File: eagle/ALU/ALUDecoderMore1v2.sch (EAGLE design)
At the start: 0 parts

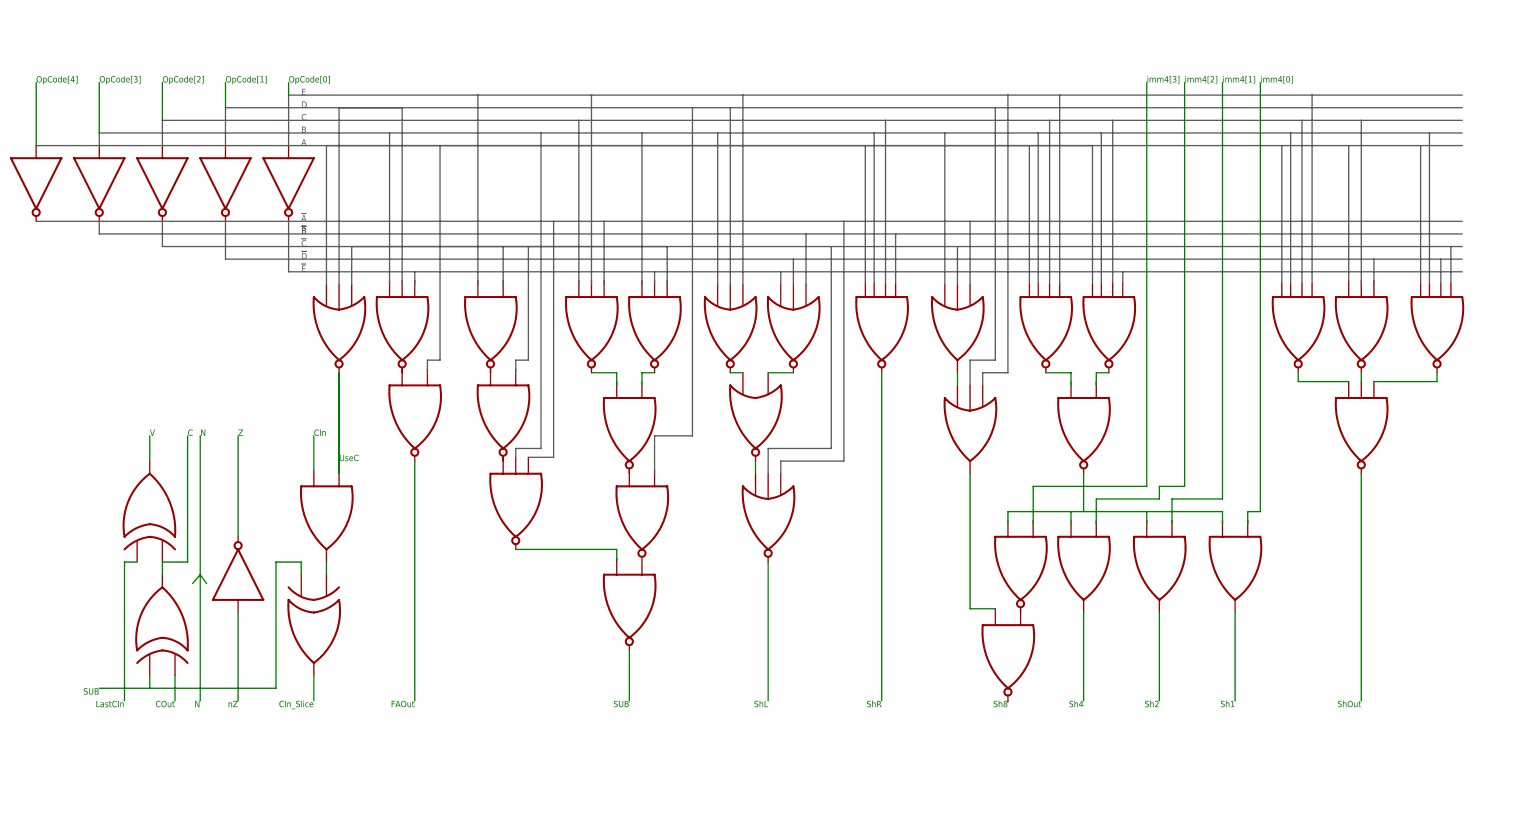
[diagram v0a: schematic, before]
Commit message: Eagle schematics now use library
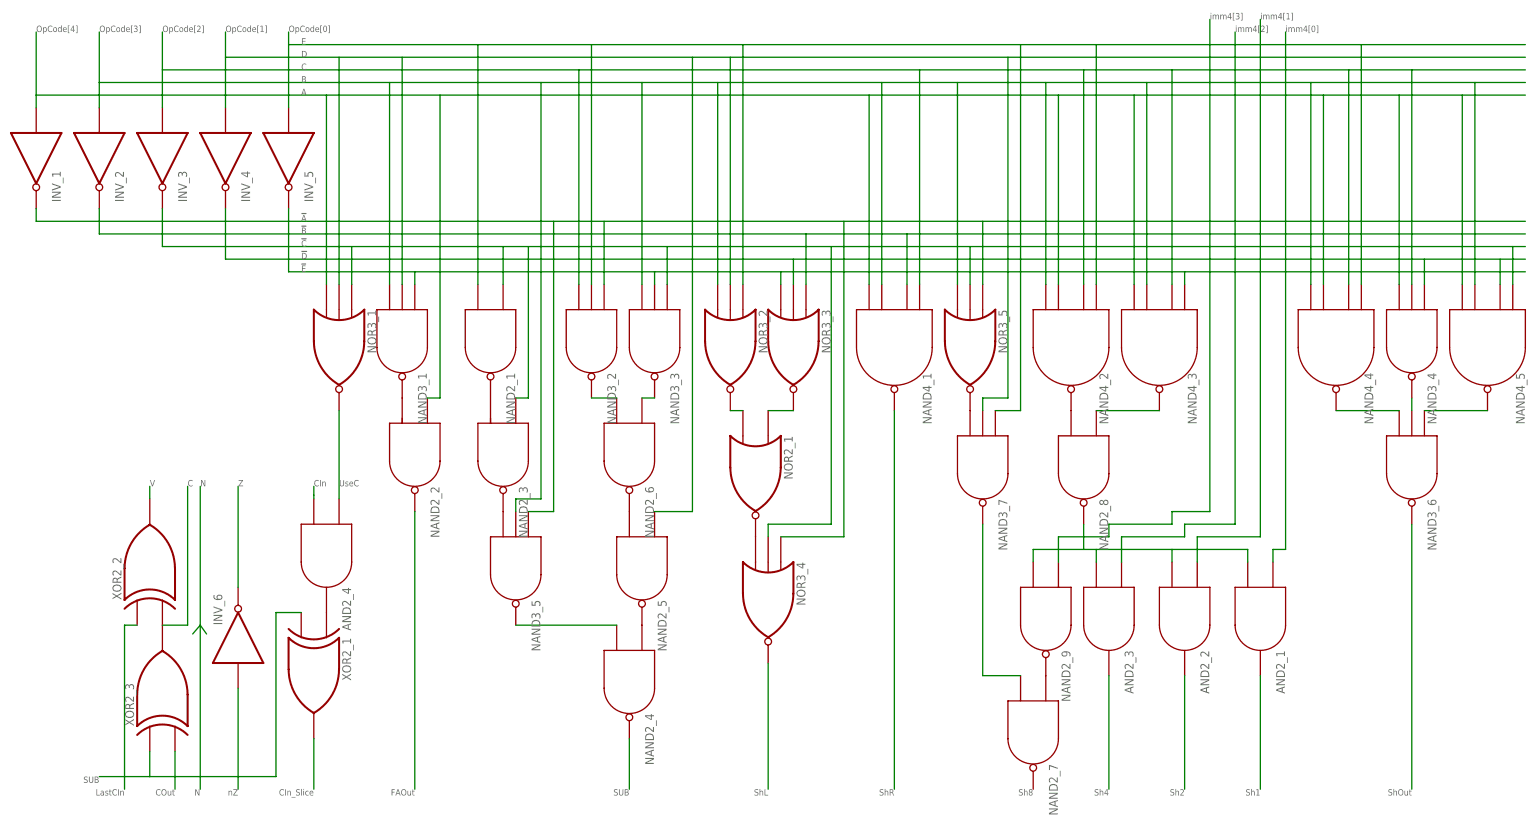
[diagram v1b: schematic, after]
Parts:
- added AND2_1, AND2_2, AND2_3, AND2_4: AND2, c035u:AND2
- added INV_1, INV_2, INV_3, INV_4, INV_5, INV_6: INV, c035u:INV
- added NAND2_1, NAND2_2, NAND2_3, NAND2_4, NAND2_5, NAND2_6, NAND2_7, NAND2_8, NAND2_9: NAND2, c035u:NAND2
- added NAND3_1, NAND3_2, NAND3_3, NAND3_4, NAND3_5, NAND3_6, NAND3_7: NAND3, c035u:NAND3
- added NAND4_1, NAND4_2, NAND4_3, NAND4_4, NAND4_5: NAND4, c035u:NAND4
- added NOR2_1: NOR2, c035u:NOR2
- added NOR3_1, NOR3_2, NOR3_3, NOR3_4, NOR3_5: NOR3, c035u:NOR3
- added XOR2_1, XOR2_2, XOR2_3: XOR2, c035u:XOR2
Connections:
- new net N$1: NAND2_1.O, NAND2_3.I1
- new net N$10: NOR2_1.I1, NOR3_2.O
- new net N$100: NAND4_4.A1
- new net N$101: NAND4_4.A
- new net N$102: NAND3_4.I1
- new net N$103: NAND3_4.I2
- new net N$104: NAND3_4.A
- new net N$105: NAND4_5.I2
- new net N$106: NAND4_5.I1
- new net N$107: NAND4_5.A1
- new net N$109: INV_2.O
- new net N$11: NOR2_1.O, NOR3_4.I1
- new net N$12: NAND2_8.I1, NAND4_2.O
- new net N$13: NAND2_8.A, NAND4_3.O
- new net N$14: NAND2_4.A, NAND2_5.O
- new net N$15: NAND2_4.O
- new net N$16: AND2_1.I1, AND2_2.I1, AND2_3.I1, NAND2_8.O, NAND2_9.I1
- new net N$17: NAND3_6.I1, NAND4_4.O
- new net N$18: NAND3_4.O, NAND3_6.I2
- new net N$19: NOR3_4.O
- new net N$2: INV_1.I
- new net N$20: NAND3_6.A, NAND4_5.O
- new net N$22: NAND3_7.I1, NOR3_5.O
- new net N$24: NAND2_9.A
- new net N$25: XOR2_2.O
- new net N$27: NAND2_7.I1, NAND3_7.O
- new net N$28: AND2_3.A
- new net N$29: AND2_2.A
- new net N$3: NAND2_2.I1, NAND3_1.O
- new net N$30: AND2_1.A
- new net N$31: AND2_3.O
- new net N$32: AND2_2.O
- new net N$33: AND2_1.O
- new net N$35: INV_6.I
- new net N$36: XOR2_3.I1
- new net N$37: NAND3_6.O
- new net N$38: XOR2_2.I1, XOR2_3.O
- new net N$39: INV_6.O
- new net N$4: NAND2_3.O, NAND3_5.I1
- new net N$40: AND2_4.I1
- new net N$41: AND2_4.A, NOR3_1.O
- new net N$42: AND2_4.O, XOR2_1.I0
- new net N$43: XOR2_1.I1, XOR2_3.I0
- new net N$44: XOR2_1.O
- new net N$45: INV_2.I
- new net N$46: INV_3.I
- new net N$47: INV_4.I
- new net N$48: INV_5.I
- new net N$49: INV_3.O, INV_4.O, INV_5.O, NAND4_5.A
- new net N$5: NAND3_5.A
- new net N$50: NAND2_4.I1, NAND3_5.O
- new net N$51: NAND2_5.I1, NAND2_6.O
- new net N$52: NAND2_7.A, NAND2_9.O
- new net N$53: INV_1.O
- new net N$54: NOR3_1.I1
- new net N$55: NOR3_1.I2
- new net N$56: NOR3_1.I0
- new net N$57: NAND3_1.I1
- new net N$58: NAND3_1.I2
- new net N$59: NAND3_1.A
- new net N$6: NAND2_6.I1, NAND3_2.O
- new net N$60: NAND2_1.I1
- new net N$61: NAND2_1.A
- new net N$62: NAND2_2.A
- new net N$63: NAND2_3.A
- new net N$65: NAND3_5.I2
- new net N$66: NAND3_2.I2
- new net N$67: NAND3_2.I1
- new net N$68: NAND3_2.A
- new net N$69: NAND3_3.I1
- new net N$7: NAND2_2.O
- new net N$70: NAND3_3.I2
- new net N$71: NAND3_3.A
- new net N$72: NAND2_5.A
- new net N$73: NOR3_2.I2
- new net N$74: NOR3_2.I1
- new net N$75: NOR3_2.I0
- new net N$76: NOR3_3.I1
- new net N$77: NOR3_3.I2
- new net N$78: NOR3_3.I0
- new net N$79: NOR3_4.I2
- new net N$8: NAND2_6.A, NAND3_3.O
- new net N$80: NOR3_4.I0
- new net N$81: NAND4_1.I2
- new net N$82: NAND4_1.I1
- new net N$84: NAND4_1.A1
- new net N$85: NOR3_5.I1
- new net N$86: NOR3_5.I0
- new net N$87: NOR3_5.I2
- new net N$88: NAND3_7.A
- new net N$89: NAND3_7.I2
- new net N$9: NOR2_1.I0, NOR3_3.O
- new net N$90: NAND4_2.I1
- new net N$91: NAND4_2.I2
- new net N$92: NAND4_2.A1
- new net N$93: NAND4_2.A
- new net N$94: NAND4_3.I2
- new net N$95: NAND4_3.I1
- new net N$96: NAND4_3.A1
- new net N$97: NAND4_3.A
- new net N$98: NAND4_4.I1
- new net N$99: NAND4_4.I2

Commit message: Schematics small improvements
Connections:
- removed net N$100: NAND4_4.A1
- removed net N$101: NAND4_4.A
- removed net N$102: NAND3_4.I1
- removed net N$103: NAND3_4.I2
- removed net N$104: NAND3_4.A
- removed net N$105: NAND4_5.I2
- removed net N$106: NAND4_5.I1
- removed net N$107: NAND4_5.A1
- removed net N$109: INV_2.O
- removed net N$2: INV_1.I
- removed net N$5: NAND3_5.A
- removed net N$54: NOR3_1.I1
- removed net N$55: NOR3_1.I2
- removed net N$56: NOR3_1.I0
- removed net N$57: NAND3_1.I1
- removed net N$58: NAND3_1.I2
- removed net N$59: NAND3_1.A
- removed net N$60: NAND2_1.I1
- removed net N$61: NAND2_1.A
- removed net N$62: NAND2_2.A
- removed net N$63: NAND2_3.A
- removed net N$65: NAND3_5.I2
- removed net N$66: NAND3_2.I2
- removed net N$67: NAND3_2.I1
- removed net N$68: NAND3_2.A
- removed net N$69: NAND3_3.I1
- removed net N$70: NAND3_3.I2
- removed net N$71: NAND3_3.A
- removed net N$72: NAND2_5.A
- removed net N$73: NOR3_2.I2
- removed net N$74: NOR3_2.I1
- removed net N$75: NOR3_2.I0
- removed net N$76: NOR3_3.I1
- removed net N$77: NOR3_3.I2
- removed net N$79: NOR3_4.I2
- removed net N$80: NOR3_4.I0
- removed net N$81: NAND4_1.I2
- removed net N$82: NAND4_1.I1
- removed net N$84: NAND4_1.A1
- removed net N$85: NOR3_5.I1
- removed net N$86: NOR3_5.I0
- removed net N$87: NOR3_5.I2
- removed net N$88: NAND3_7.A
- removed net N$89: NAND3_7.I2
- removed net N$90: NAND4_2.I1
- removed net N$91: NAND4_2.I2
- removed net N$92: NAND4_2.A1
- removed net N$93: NAND4_2.A
- removed net N$95: NAND4_3.I1
- removed net N$96: NAND4_3.A1
- removed net N$97: NAND4_3.A
- removed net N$98: NAND4_4.I1
- removed net N$99: NAND4_4.I2
- net N$49: now also NAND2_1.A, NAND2_3.A, NAND3_1.A, NAND3_3.A, NAND3_3.I2, NAND3_4.A, NAND4_3.A, NAND4_5.A1, NOR3_1.I0, NOR3_3.I1, NOR3_3.I2, NOR3_4.I2, NOR3_5.I2
- net N$53: now also NAND3_2.A, NAND3_5.A, NOR3_4.I0, NOR3_5.I0
- net N$78: now also INV_2.O, NAND4_1.A1
- net N$94: now also INV_1.I, NAND2_1.I1, NAND2_2.A, NAND2_5.A, NAND3_1.I1, NAND3_1.I2, NAND3_2.I1, NAND3_2.I2, NAND3_3.I1, NAND3_4.I1, NAND3_4.I2, NAND3_5.I2, NAND3_7.A, NAND3_7.I2, NAND4_1.I1, NAND4_1.I2, NAND4_2.A, NAND4_2.A1, NAND4_2.I1, NAND4_2.I2, NAND4_3.A1, NAND4_3.I1, NAND4_4.A, NAND4_4.A1, NAND4_4.I1, NAND4_4.I2, NAND4_5.I1, NAND4_5.I2, NOR3_1.I1, NOR3_1.I2, NOR3_2.I0, NOR3_2.I1, NOR3_2.I2, NOR3_5.I1
